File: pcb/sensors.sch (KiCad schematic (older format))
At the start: 2 parts, among them U3 LSM330DLC

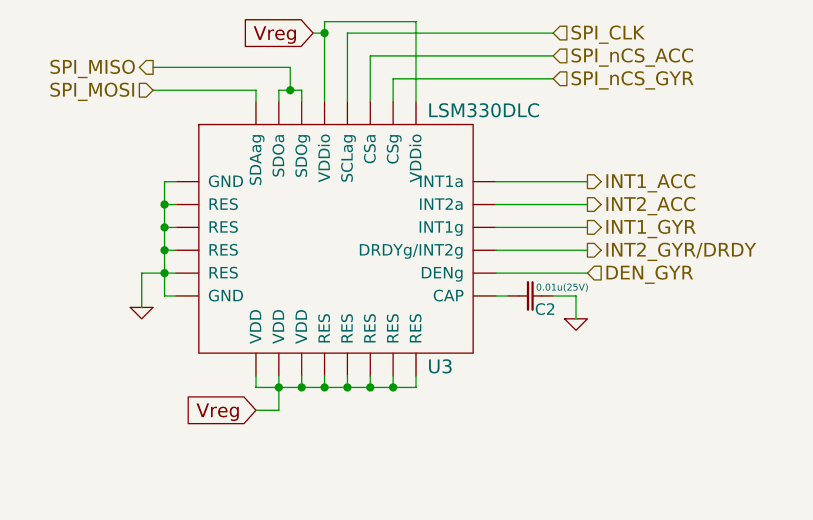
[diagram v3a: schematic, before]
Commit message: Added two capacitors to the sensor modules.
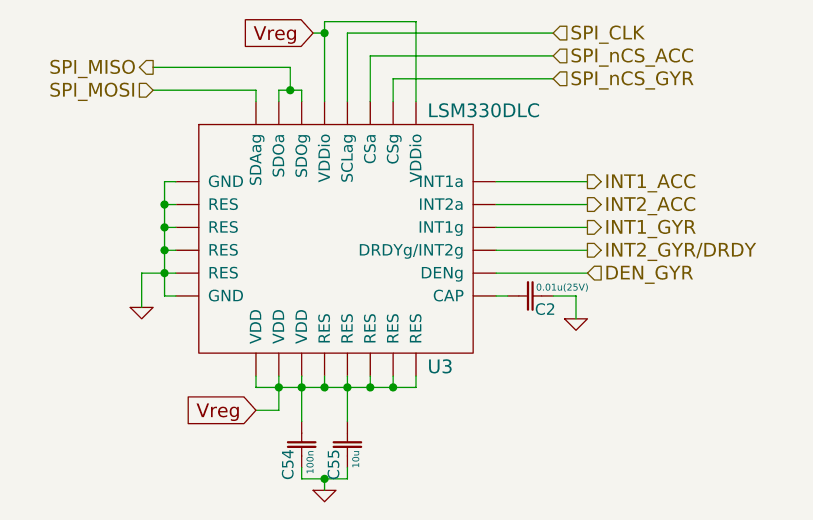
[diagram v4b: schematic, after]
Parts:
- added C54: 100n, symbol CAP
- added C55: 10u, symbol CAP
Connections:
- net GND: now also C54.2, C55.2
- net Vreg: now also C54.1, C55.1
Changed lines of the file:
@@
-EESchema Schematic File Version 2  date Mon 21 Jan 2013 04:13:24 PM EST
+EESchema Schematic File Version 2  date Mon 21 Jan 2013 04:46:11 PM EST
 LIBS:power
 LIBS:device
@@
 Comment4 ""
 $EndDescr
+$Comp
+L GND #PWR016
+U 1 1 50FDB46B
+P 5450 4950
+F 0 "#PWR016" H 5450 4950 30  0001 C CNN
+F 1 "GND" H 5450 4880 30  0001 C CNN
+	1    5450 4950
+	1    0    0    -1
+$EndComp
+Connection ~ 5450 4900
+Wire Wire Line
+	5450 4900 5450 4950
+Wire Wire Line
+	5550 4650 5550 4450
 Wire Wire Line
 	6600 4000 6200 4000
@@
 	5650 4500 5650 4450
 Connection ~ 5550 4500
-Wire Wire Line
-	5550 4500 5550 4450
 Connection ~ 5750 4500
 Wire Wire Line
@@
 	5150 4500 5150 4450
 Connection ~ 5450 4500
-Wire Wire Line
-	5350 4500 5350 4450
 Connection ~ 5350 4500
 Wire Wire Line
@@
 Wire Wire Line
 	6600 3900 6200 3900
+Wire Wire Line
+	5350 4650 5350 4450
+Wire Wire Line
+	5550 4850 5550 4900
+Wire Wire Line
+	5550 4900 5350 4900
+Wire Wire Line
+	5350 4900 5350 4850
+$Comp
+L CAP C55
+U 1 1 50FDB43C
+P 5550 4750
+F 0 "C55" H 5570 4720 50  0000 L TNN
+F 1 "10u" H 5575 4770 30  0000 L BNN
+	1    5550 4750
+	0    1    1    0
+$EndComp
+$Comp
+L CAP C54
+U 1 1 50FDB421
+P 5350 4750
+F 0 "C54" H 5370 4720 50  0000 L TNN
+F 1 "100n" H 5375 4770 30  0000 L BNN
+	1    5350 4750
+	0    1    1    0
+$EndComp
 Text HLabel 6600 4000 2    60   Input ~ 0
 DEN_GYR
@@
 $EndComp
 $Comp
-L GND #PWR016
+L GND #PWR017
 U 1 1 50C11356
 P 4650 4150
-F 0 "#PWR016" H 4650 4150 30  0001 C CNN
+F 0 "#PWR017" H 4650 4150 30  0001 C CNN
 F 1 "GND" H 4650 4080 30  0001 C CNN
 	1    4650 4150
@@
 $EndComp
 $Comp
-L GND #PWR017
+L GND #PWR018
 U 1 1 50C11354
 P 6550 4200
-F 0 "#PWR017" H 6550 4200 30  0001 C CNN
+F 0 "#PWR018" H 6550 4200 30  0001 C CNN
 F 1 "GND" H 6550 4130 30  0001 C CNN
 	1    6550 4200
